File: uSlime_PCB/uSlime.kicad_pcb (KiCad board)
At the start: 2 copper layers, 25 x 22.6 mm, 46 parts, among them CN1 1.25T-2AW, CN2 X1502WR-05K-N0SN, J1 USB_C_Receptacle_USB2.0_14P, U1 MCP73831T-2ACI/OT, U2 MSK-12C02_SMD_SPDT_SWITCH, U3 AP2112K-3.3TRG1, U4 ESP32-C6-MINI-1, U5 BNO085

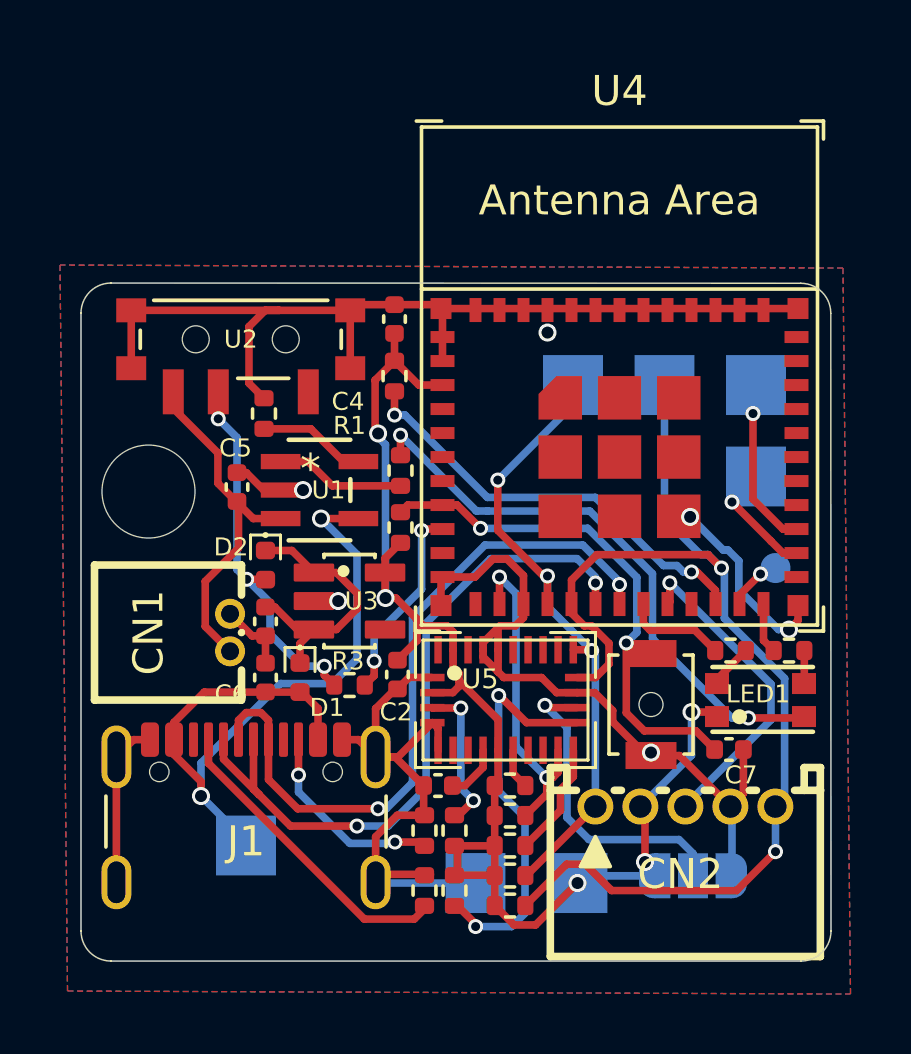
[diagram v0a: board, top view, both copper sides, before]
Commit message: Add JLCPCB associated parts
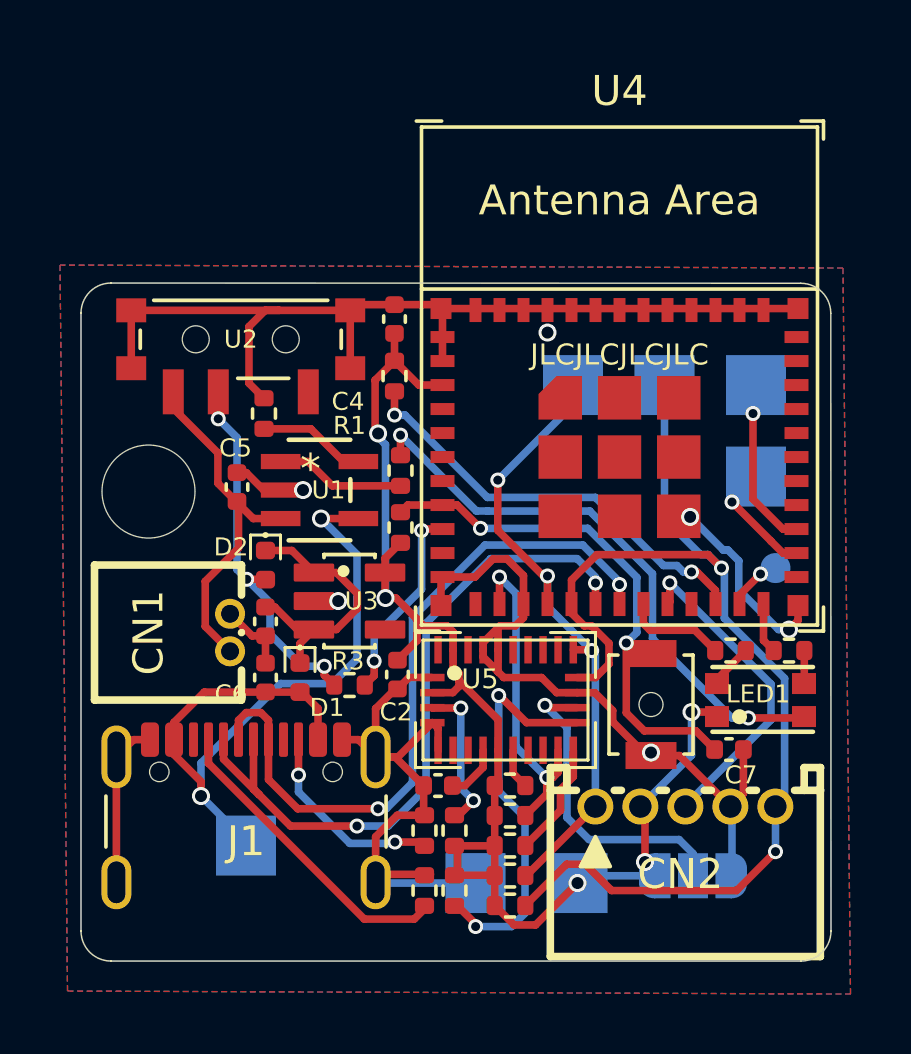
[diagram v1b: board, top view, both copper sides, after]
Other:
- board text added: "JLCJLCJLCJLC"

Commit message: Change charge LED to 2.2k, always on light if not charging
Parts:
- R9: value 1k -> 2.2k
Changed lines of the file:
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@@
 			)
 		)
-		(property "Value" "1k"
+		(property "Value" "2.2k"
 			(at 0 1.17 -90)
 			(layer "F.Fab")
@@
 		(name "$teardrop_padvia$")
 		(hatch full 0.1)
-		(priority 30005)
-		(attr
-			(teardrop
-				(type padvia)
-			)
-		)
-		(connect_pads yes
-			(clearance 0)
-		)
-		(min_thickness 0.0254)
-		(filled_areas_thickness no)
-		(fill yes
-			(thermal_gap 0.5)
-			(thermal_bridge_width 0.5)
-			(island_removal_mode 1)
-			(island_area_min 10)
-		)
-		(polygon
-			(pts
-				(xy 110.912 99.252984) (xy 110.658 99.252984) (xy 110.522836 99.735195) (xy 110.8 99.851) (xy 111.077164 99.735195)
-			)
-		)
-	)
-	(zone
-		(net 15)
-		(net_name "D+ P")
-		(layer "F.Cu")
-		(name "$teardrop_padvia$")
-		(hatch full 0.1)
-		(priority 30020)
-		(attr
-			(teardrop
-				(type padvia)
-			)
-		)
-		(connect_pads yes
-			(clearance 0)
-		)
-		(min_thickness 0.0254)
-		(filled_areas_thickness no)
-		(fill yes
-			(thermal_gap 0.5)
-			(thermal_bridge_width 0.5)
-			(island_removal_mode 1)
-			(island_area_min 10)
-		)
-		(polygon
-			(pts
-				(xy 118.473 99.9) (xy 118.727 99.9) (xy 118.83097 99.495671) (xy 118.6 99.399) (xy 118.36903 99.495671)
-			)
-		)
-	)
-	(zone
-		(net 43)
-		(net_name "Net-(D2-A)")
-		(layer "F.Cu")
-		(name "$teardrop_padvia$")
-		(hatch full 0.1)
-		(priority 30015)
-		(attr
-			(teardrop
-				(type padvia)
-			)
-		)
-		(connect_pads yes
-			(clearance 0)
-		)
-		(min_thickness 0.0254)
-		(filled_areas_thickness no)
-		(fill yes
-			(thermal_gap 0.5)
-			(thermal_bridge_width 0.5)
-			(island_removal_mode 1)
-			(island_area_min 10)
-		)
-		(polygon
-			(pts
-				(xy 105.352 93.375) (xy 105.098 93.375) (xy 104.99403 93.779329) (xy 105.225 93.876) (xy 105.45597 93.779329)
-			)
-		)
-	)
-	(zone
-		(net 34)
-		(net_name "+3.3V")
-		(layer "F.Cu")
-		(name "$teardrop_padvia$")
-		(hatch full 0.1)
 		(priority 30001)
 		(attr
@@
 		(name "$teardrop_padvia$")
 		(hatch full 0.1)
-		(priority 30004)
-		(attr
-			(teardrop
-				(type padvia)
-			)
-		)
-		(connect_pads yes
-			(clearance 0)
-		)
-		(min_thickness 0.0254)
-		(filled_areas_thickness no)
-		(fill yes
-			(thermal_gap 0.5)
-			(thermal_bridge_width 0.5)
-			(island_removal_mode 1)
-			(island_area_min 10)
-		)
-		(polygon
-			(pts
-				(xy 108.623 99.823) (xy 108.623 100.077) (xy 109.108195 100.227164) (xy 109.224 99.95) (xy 109.108195 99.672836)
-			)
-		)
-	)
-	(zone
-		(net 1)
-		(net_name "GND")
-		(layer "F.Cu")
-		(name "$teardrop_padvia$")
-		(hatch full 0.1)
 		(priority 30003)
 		(attr
@@
 	)
 	(zone
-		(net 36)
-		(net_name "BatSense")
-		(layer "F.Cu")
-		(name "$teardrop_padvia$")
-		(hatch full 0.1)
-		(priority 30013)
-		(attr
-			(teardrop
-				(type padvia)
-			)
-		)
-		(connect_pads yes
-			(clearance 0)
-		)
-		(min_thickness 0.0254)
-		(filled_areas_thickness no)
-		(fill yes
-			(thermal_gap 0.5)
-			(thermal_bridge_width 0.5)
-			(island_removal_mode 1)
-			(island_area_min 10)
-		)
-		(polygon
-			(pts
-				(xy 112.492546 97.677) (xy 112.492546 97.423) (xy 112.002002 97.347538) (xy 112.001002 97.597538)
-				(xy 112.097673 97.828508)
-			)
-		)
-	)
-	(zone
 		(net 5)
 		(net_name "VBUS")
@@
 			)
 		)
-	)
-	(zone
-		(net 18)
-		(net_name "D- N")
-		(layer "F.Cu")
-		(name "$teardrop_padvia$")
-		(hatch full 0.1)
-		(priority 30019)
-		(attr
-			(teardrop
-				(type padvia)
-			)
-		)
-		(connect_pads yes
-			(clearance 0)
-		)
-		(min_thickness 0.0254)
-		(filled_areas_thickness no)
-		(fill yes
-			(thermal_gap 0.5)
-			(thermal_bridge_width 0.5)
-			(island_removal_mode 1)
-			(island_area_min 10)
-		)
-		(polygon
-			(pts
-				(xy 117.673 99.85) (xy 117.927 99.85) (xy 118.03097 99.445671) (xy 117.8 99.349) (xy 117.56903 99.445671)
-			)
-		)

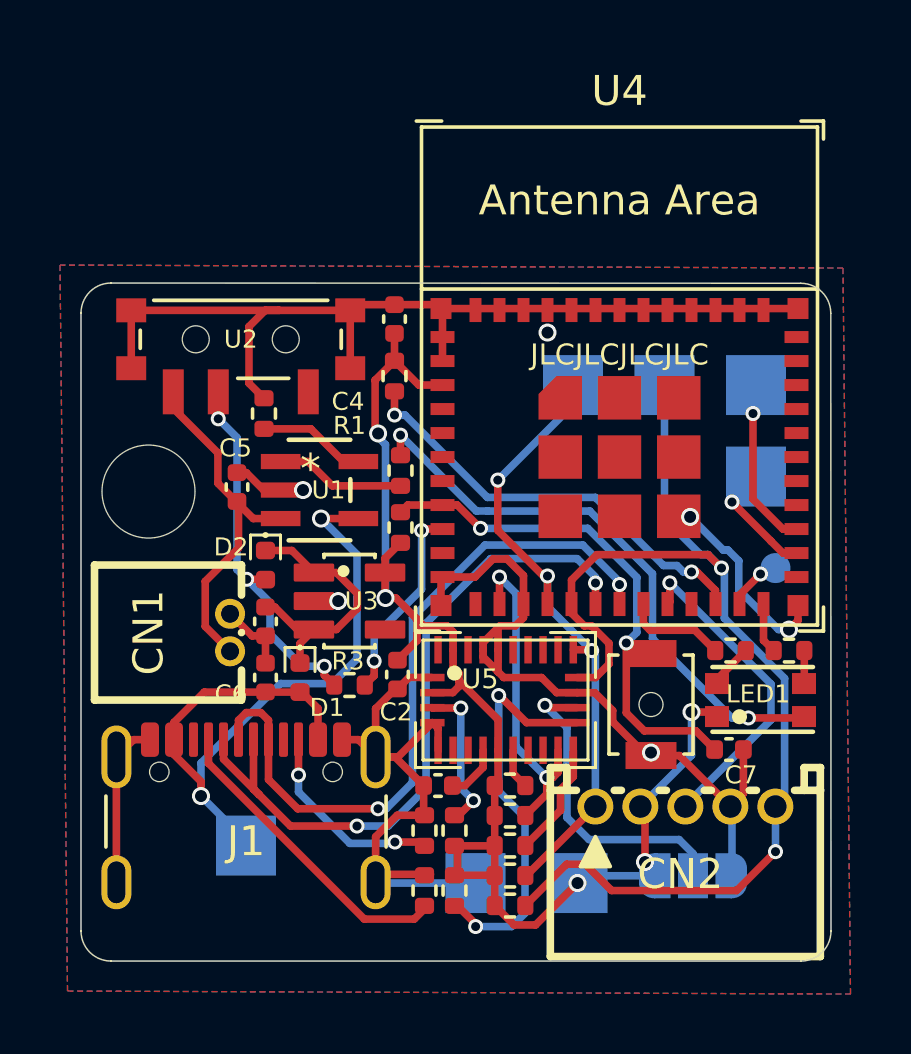
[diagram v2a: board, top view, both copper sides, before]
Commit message: v1.1.0 - Add 603 LED and resistor for charger status
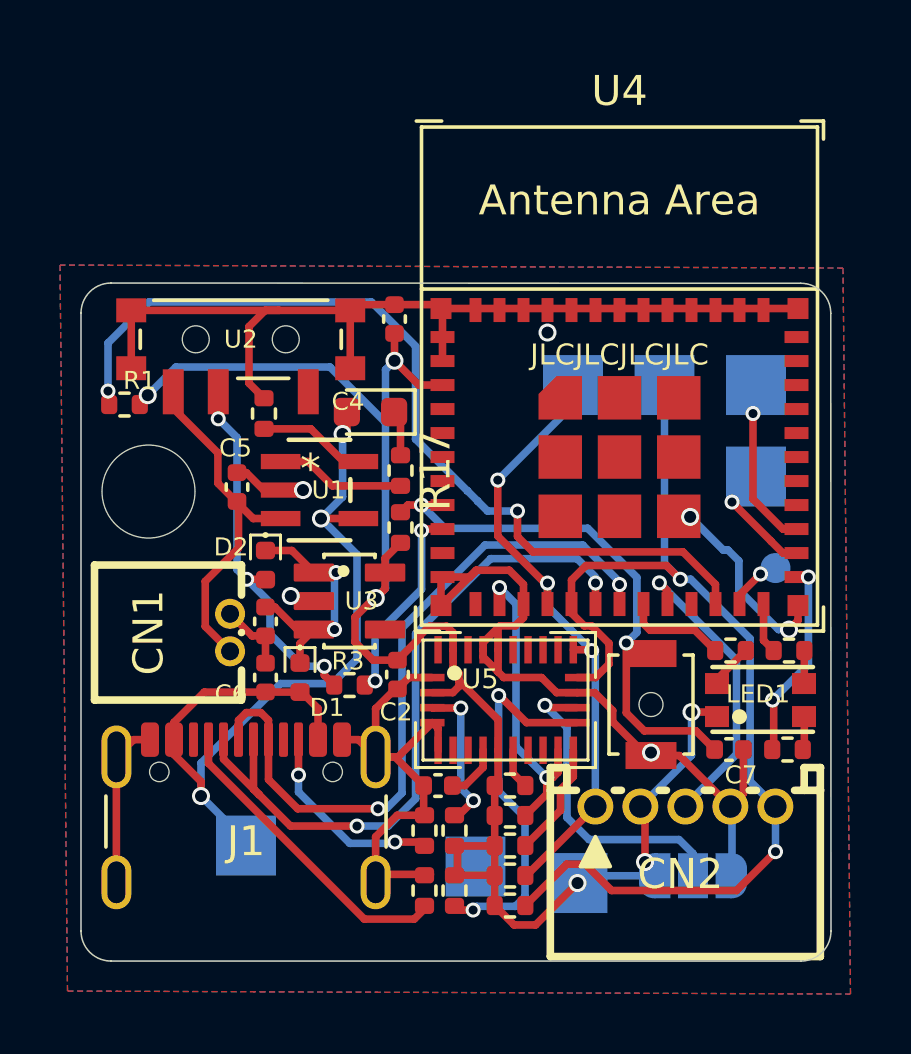
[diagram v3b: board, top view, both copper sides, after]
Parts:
- added D3: D, Diode_SMD:D_0603_1608Metric, F.Cu at (110.3, 93.7)
- added R17: 1k, Resistor_SMD:R_0402_1005Metric, F.Cu at (111.3, 95.6)
- R9: value 2.2k -> 1k
- moved R9 15.9 mm to (124.2, 104.9), turned to 0 degrees
- moved R1 9.05 mm to (102.1, 93.4), turned to 0 degrees
- moved TP7 0.55 mm to (113.8, 108.8)
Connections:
- R9 pad 1: STAT -> /ESP32-C6FH4/IO19/SCK
- U1 pad 1: STAT -> Net-(U1-STAT)
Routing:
- net Net-(LED1---Pad4): track 19.3 -> 1.10 mm, vias 2 -> 0
- net /ESP32-C6FH4/IO8: track 14.4 -> 29.8 mm
- net +3.3V: track 45.7 -> 56.6 mm, vias 5 -> 6
- net /ESP32-C6FH4/IO19/SCK: track 0.00 -> 6.66 mm, vias 0 -> 2
- net STAT: track 4.33 -> 0.00 mm
- net Net-(U1-STAT): track 0.00 -> 4.33 mm
- net VBUS: track 25.7 -> 29.6 mm, vias 2 -> 3
- net GND: track 93.9 -> 91.8 mm
- net BNO_SCL: track 37.5 -> 35.8 mm
- net Net-(D3-K): track 0.00 -> 1.53 mm
- net /ESP32-C6FH4/ESP_EN: track 18.2 -> 19.6 mm
- net Net-(U5-ENV_SDA): track 13.4 -> 12.5 mm
- net BNO_INT2: track 10.8 -> 10.0 mm
- net BNO_INT: track 11.0 -> 10.3 mm
- net Net-(D1-K): track 9.55 -> 8.92 mm, vias 0 -> 2
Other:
- board text added: "v1.1.0"
- board text removed: "v1.0.0"

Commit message: Forgot to change silkscreen positions
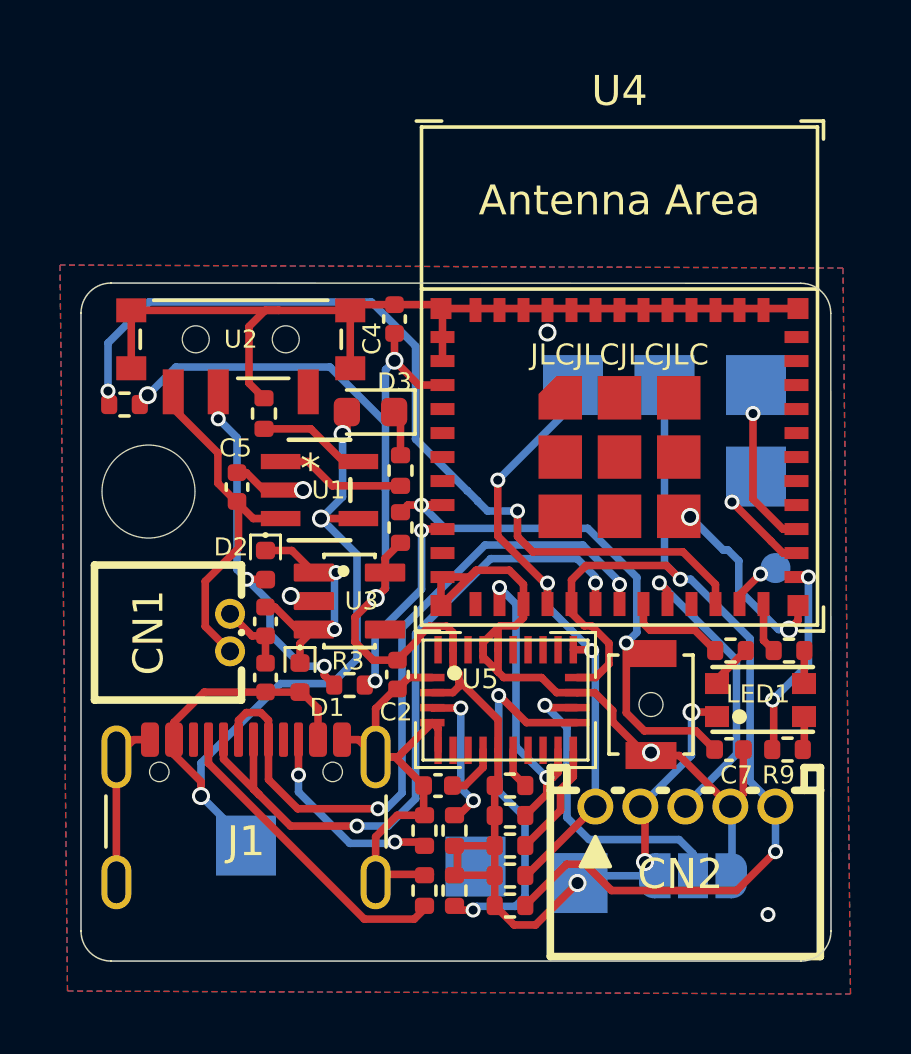
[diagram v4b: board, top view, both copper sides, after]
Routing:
- net GND: vias 6 -> 7

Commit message: v1.2.0 - Refactor component placement and electrical accuracy
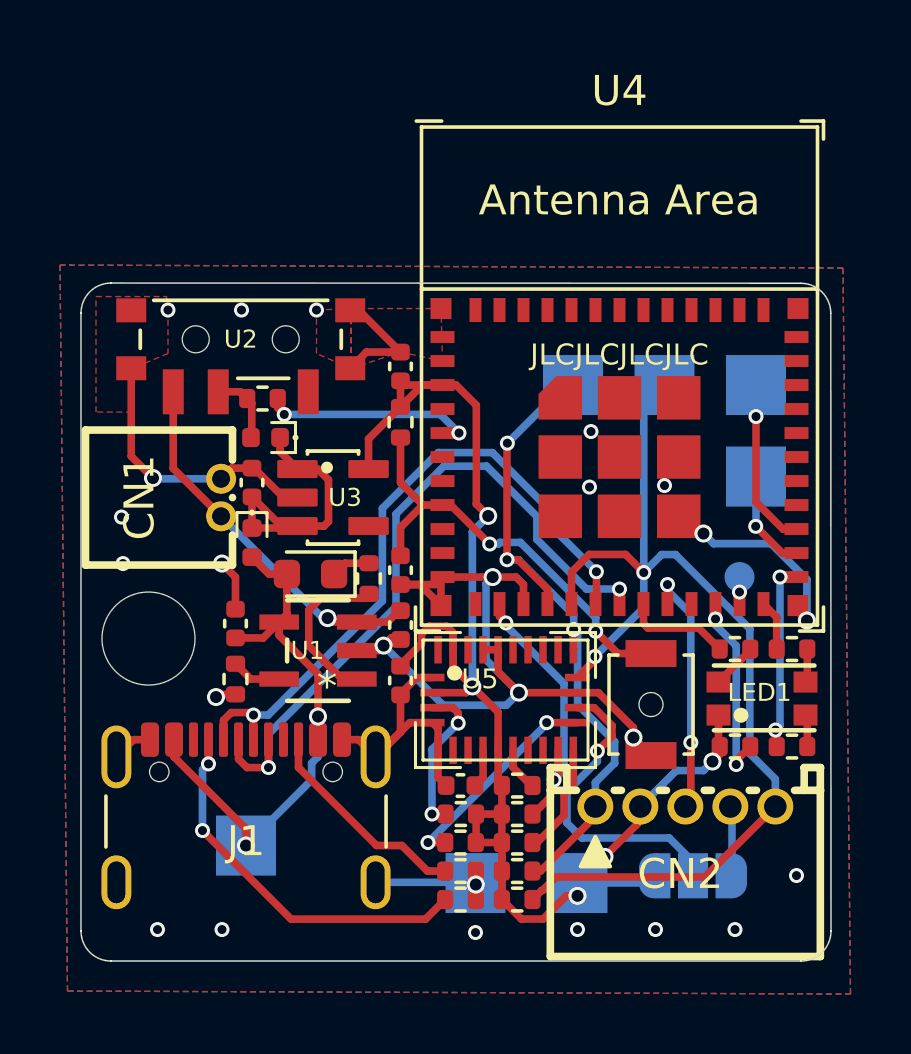
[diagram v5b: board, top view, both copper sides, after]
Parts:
- moved R1 23.3 mm to (122.5, 104.8), turned to 180 degrees
- moved C7 12.5 mm to (111.3, 98.9), turned to -90 degrees
- moved R3 9.98 mm to (106.7, 93.2)
- moved R2 8.90 mm to (105.8, 102.5), turned to -90 degrees
- moved C5 7.13 mm to (111.3, 100.8), turned to -90 degrees
- moved D3 5.76 mm to (108.3, 99.0)
- moved U1 5.35 mm to (108.5, 101.6), turned to 180 degrees
- moved ? 4.90 mm to (102.9, 101.2)
- moved D1 4.78 mm to (106.3, 98.0)
- moved C3 4.65 mm to (106.3, 96.0), turned to 90 degrees
- moved CN1 4.51 mm to (105.3, 96.5)
- moved D2 4.25 mm to (106.8, 94.5), turned to 180 degrees
- moved R17 3.75 mm to (110.2, 99.2)
- moved R6 3.51 mm to (111.3, 94.0), turned to 90 degrees
- moved U3 3.49 mm to (109.0, 96.5)
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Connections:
- U4 pad 5: /ESP32-C6FH4/IO2 -> BatSense
- U4 pad 9: BatSense -> /ESP32-C6FH4/IO4
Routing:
- net GND: track 91.8 -> 66.5 mm, vias 7 -> 25
- net /ESP32-C6FH4/IO8: track 29.8 -> 6.43 mm
- net VBUS: track 29.6 -> 19.1 mm, vias 3 -> 2
- net Net-(D2-A): track 12.4 -> 2.64 mm, vias 3 -> 0
- net +3.3V: track 56.6 -> 47.0 mm, vias 6 -> 5
- net Net-(U5-ENV_SDA): track 12.5 -> 7.22 mm
- net /ESP32-C6FH4/ESP_EN: track 19.6 -> 14.5 mm
- net Net-(J1-CC1): track 10.4 -> 12.7 mm, vias 0 -> 2
- net BNO_SDA: track 21.1 -> 23.2 mm
- net Net-(U1-PROG): track 3.60 -> 1.67 mm
- net BNO_INT2: track 10.0 -> 8.45 mm, vias 1 -> 2
- net D- N: track 23.8 -> 22.5 mm
- net Net-(U1-STAT): track 4.33 -> 5.48 mm
- net /ESP32-C6FH4/IO9/BOOT: track 1.87 -> 0.90 mm
- net VBAT: track 11.6 -> 12.4 mm, vias 0 -> 1
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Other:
- board text added: "v1.2.0"
- board text removed: "v1.1.0"
